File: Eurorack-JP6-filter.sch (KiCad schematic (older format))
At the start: 138 parts, among them J1 JACK_MONO_SW, J2 JACK_MONO_SW, J3 JACK_MONO_SW, J4 JACK_MONO_SW, J5 JACK_MONO_SW, J6 JACK_MONO_SW, P1 CONN_02X05, Q1 BCM857BS, Q2 BCM857BS, Q3 J112, Q4 J112, Q5 J112, Q6 J112, SW1 KS-01Q, U1 TL072-, U10 CD4027, U11 CD40106, U2 TL072-, U3 TL072-, U4 TL072-, U5 LM13700, U6 LM13700, U7 LM13700, U8 DG409, U9 CD4052

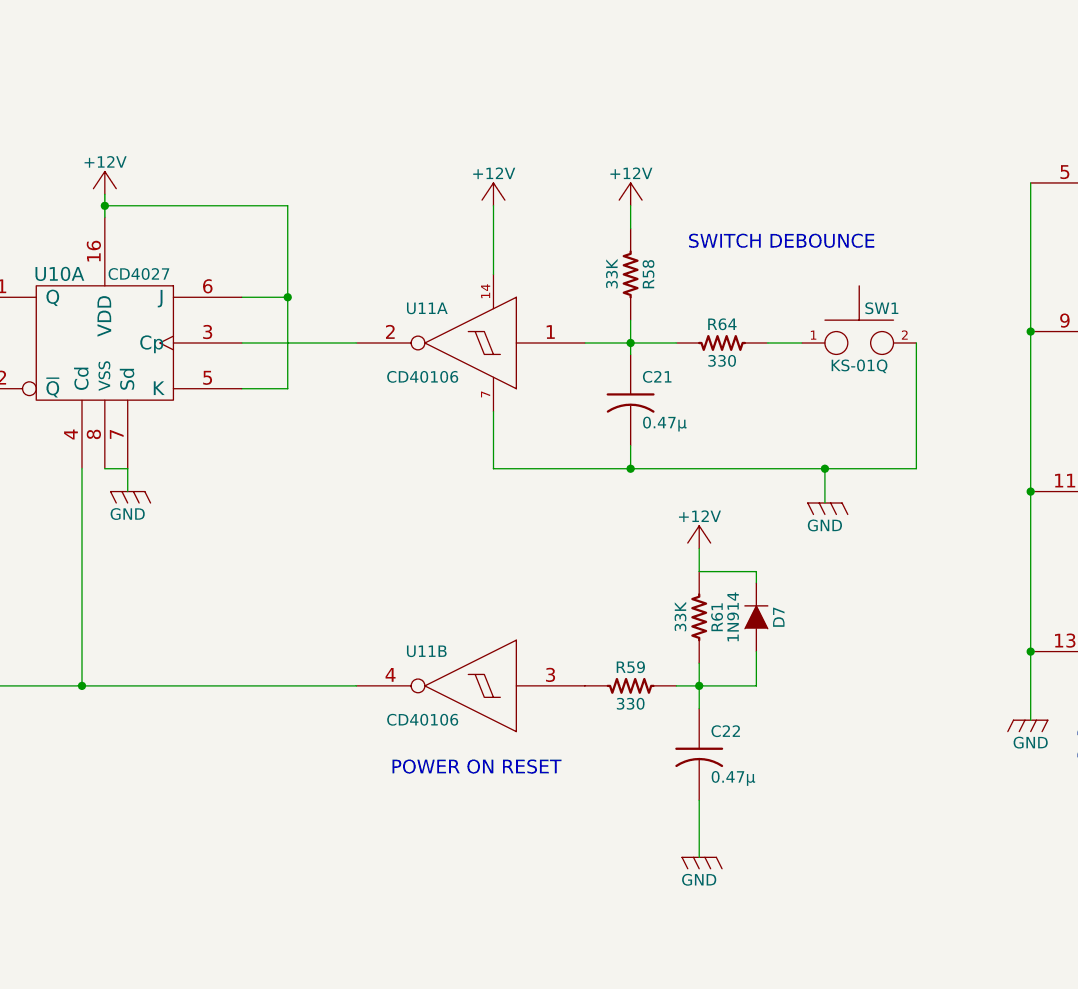
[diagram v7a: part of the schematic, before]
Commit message: routing power, swapped units on hex inverter
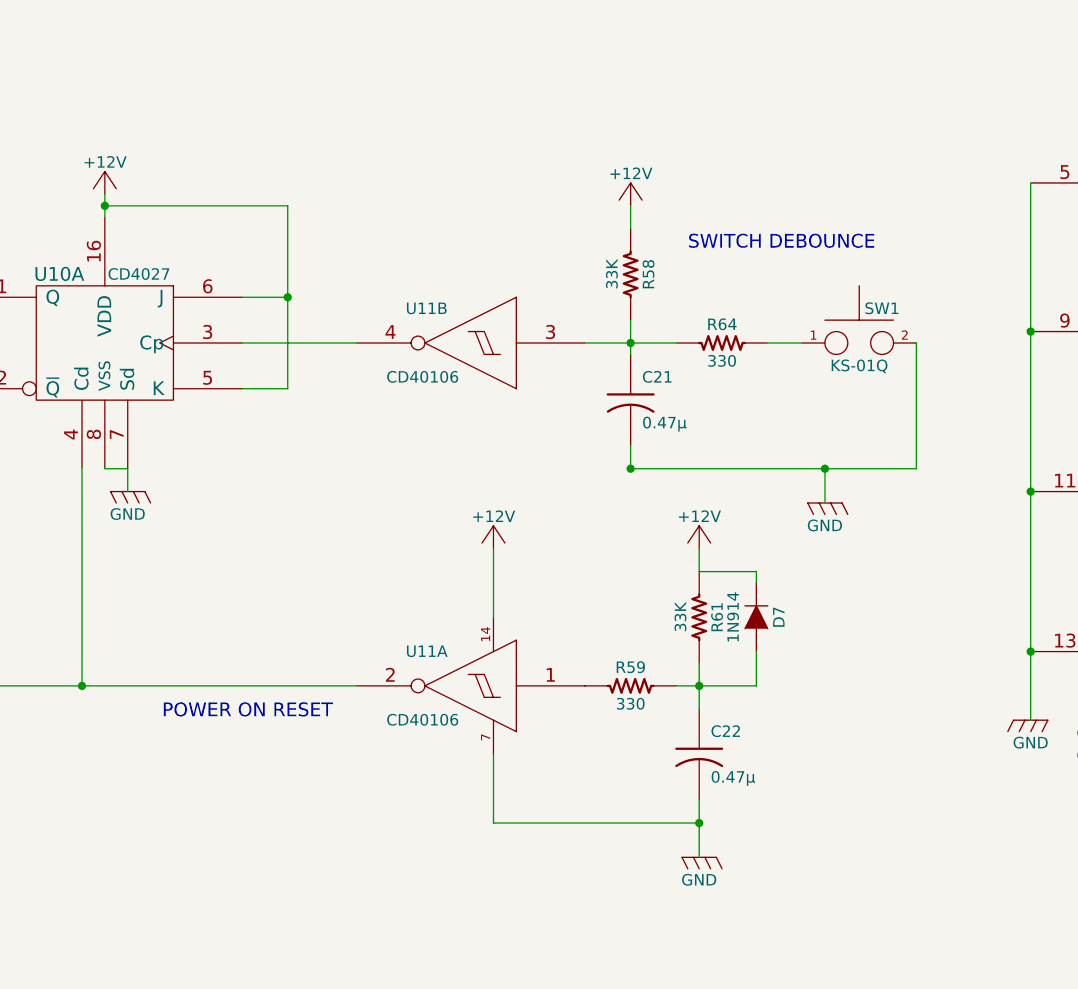
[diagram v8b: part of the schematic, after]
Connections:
- net +12V: now also U11.14 (VDD); no longer U11.14 (VDD)
- net GND: now also U11.7 (VSS); no longer U11.7 (VSS)
- net at C21.1, R58.1, R64.1: now also U11.3 (In); no longer U11.1 (In)
- net at U10.3 (Cp): now also U11.4 (Out); no longer U11.2 (Out)
- net at U10.12 (Cd), U10.4 (Cd): now also U11.2 (Out); no longer U11.4 (Out)
- net at R59.1: now also U11.1 (In); no longer U11.3 (In)
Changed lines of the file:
@@
 L +12V #PWR078
 U 1 1 5547ACDA
-P 16700 4550
-F 0 "#PWR078" H 16700 4400 50  0001 C CNN
-F 1 "+12V" H 16700 4690 50  0000 C CNN
-F 2 "" H 16700 4550 60  0000 C CNN
-F 3 "" H 16700 4550 60  0000 C CNN
-	1    16700 4550
+P 16700 6050
+F 0 "#PWR078" H 16700 5900 50  0001 C CNN
+F 1 "+12V" H 16700 6190 50  0000 C CNN
+F 2 "" H 16700 6050 60  0000 C CNN
+F 3 "" H 16700 6050 60  0000 C CNN
+	1    16700 6050
 	-1   0    0    -1
 $EndComp
@@
 	-1   0    0    -1
 $EndComp
-Text Notes 16250 7050 0    60   ~ 0
+Text Notes 15250 6800 0    60   ~ 0
 POWER ON RESET
 Text Notes 17550 4750 0    60   ~ 0
@@
 $Comp
 L CD40106 U11
-U 1 1 5549492A
+U 2 1 5549492A
 P 16600 5150
 F 0 "U11" H 16700 5300 50  0000 L CNN
@@
 F 2 "Housings_SSOP:TSSOP-14_4.4x5mm_Pitch0.65mm" H 16600 5150 60  0001 C CNN
 F 3 "" H 16600 5150 60  0000 C CNN
-	1    16600 5150
+	2    16600 5150
 	-1   0    0    -1
 $EndComp
 $Comp
 L CD40106 U11
-U 2 1 5549577D
+U 1 1 5549577D
 P 16600 6650
 F 0 "U11" H 16700 6800 50  0000 L CNN
@@
 F 2 "Housings_SSOP:TSSOP-14_4.4x5mm_Pitch0.65mm" H 16600 6650 60  0001 C CNN
 F 3 "" H 16600 6650 60  0000 C CNN
-	2    16600 6650
+	1    16600 6650
 	-1   0    0    -1
 $EndComp
@@
 	18550 5700 18550 5150
 Wire Wire Line
-	16700 5700 18550 5700
-Wire Wire Line
 	17300 5700 17300 5600
 Wire Wire Line
@@
 Wire Wire Line
 	12050 4800 11600 4800
-Wire Wire Line
-	16700 5700 16700 5450
 Connection ~ 17300 5700
 Wire Wire Line
-	16700 4850 16700 4550
+	16700 6350 16700 6050
 Wire Wire Line
 	17100 5150 17500 5150
@@
 Wire Wire Line
 	14350 15400 14350 15600
+Wire Wire Line
+	16700 6950 16700 7250
+Wire Wire Line
+	16700 7250 17600 7250
+Connection ~ 17600 7250
+Wire Wire Line
+	17300 5700 18550 5700
 $EndSCHEMATC
